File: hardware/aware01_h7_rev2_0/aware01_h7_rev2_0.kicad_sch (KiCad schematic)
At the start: 43 parts, among them J1 Conn_02x07_Odd_Even, J2 Conn_02x05_Odd_Even, U1 LMR50410Y5FQDBVRQ1, U2 LM1117MP-3.3, U4 STM32H7A3RITx, U5 LM4040DIM3X-10, Y1 WE-XTAL 24.0MHz 50ppm

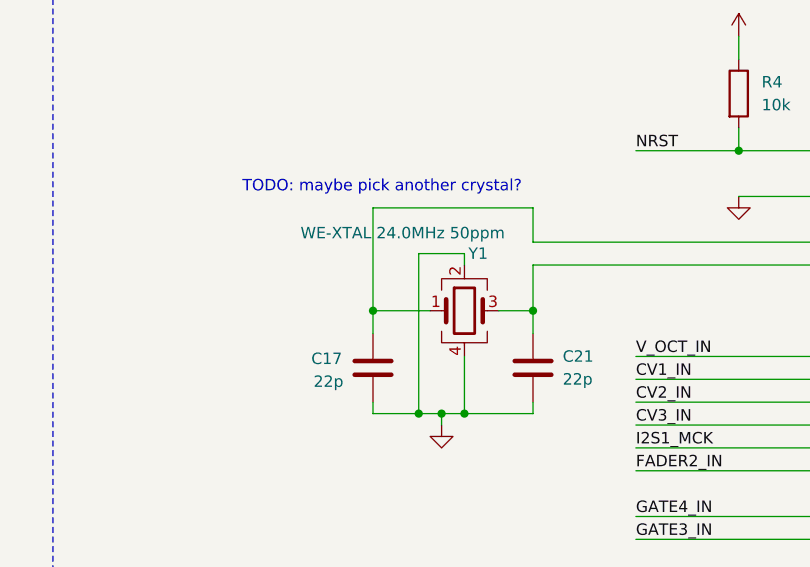
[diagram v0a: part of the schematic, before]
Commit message: hardware: switch crystal and calculate load caps
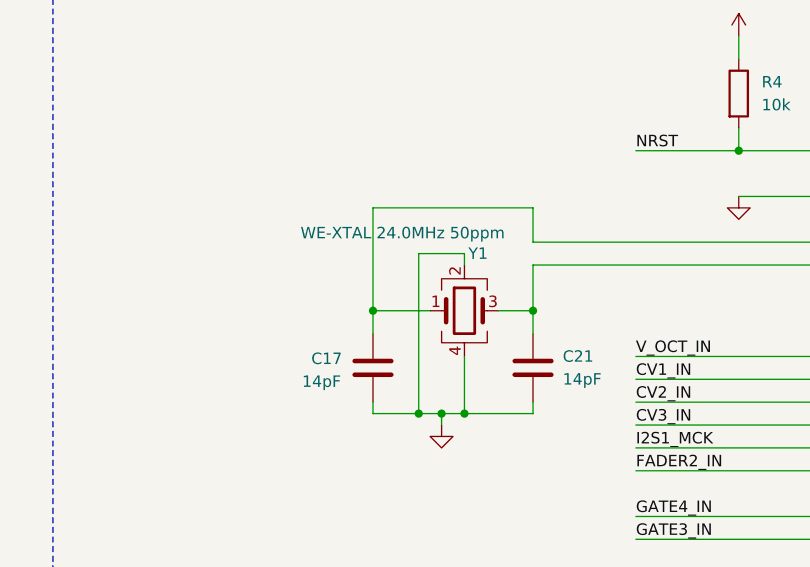
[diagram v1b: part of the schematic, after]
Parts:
- C17, C21: value 22p -> 14pF; footprint Capacitor_SMD:C_0603_1608Metric -> Capacitor_SMD:C_0402_1005Metric_Pad0.74x0.62mm_HandSolder; Manufacturer_Name KEMET -> KYOCERA AVX; Manufacturer_Part_Number C0603C220J1GACTU -> 04023U140GAT2A; Mouser Part Number 80-C0603C220J1G -> 581-04023U140GAT2A
- Y1: footprint Crystal:Crystal_SMD_3225-4Pin_3.2x2.5mm_HandSoldering -> Crystal:Crystal_SMD_2520-4Pin_2.5x2.0mm; Manufacturer_Name Wurth Elektronik -> NDK; Manufacturer_Part_Number 830064703 -> NX2520SA-24.000000MHZ-B8; Mouser Part Number 710-830064703 -> 344-NX2520SA24MHZB8
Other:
- note removed: "TODO: maybe pick another crystal?"
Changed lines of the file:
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@@
 		)
 	)
-	(text "TODO: maybe pick another crystal?"
-		(exclude_from_sim no)
-		(at 150.876 117.094 0)
-		(effects
-			(font
-				(size 1.27 1.27)
-			)
-		)
-	)
 	(text "Power Regulators"
 		(exclude_from_sim no)
@@
 			)
 		)
-		(property "Value" "22p"
-			(at 143.256 138.684 0)
+		(property "Value" "14pF"
+			(at 141.986 138.684 0)
 			(effects
 				(font
@@
 			)
 		)
-		(property "Footprint" "Capacitor_SMD:C_0603_1608Metric"
+		(property "Footprint" "Capacitor_SMD:C_0402_1005Metric_Pad0.74x0.62mm_HandSolder"
 			(at 150.8252 140.97 0)
 			(effects
@@
 			)
 		)
-		(property "Manufacturer_Name" "KEMET "
+		(property "Manufacturer_Name" "KYOCERA AVX "
 			(at 149.86 137.16 0)
 			(effects
@@
 			)
 		)
-		(property "Manufacturer_Part_Number" " C0603C220J1GACTU"
+		(property "Manufacturer_Part_Number" " 04023U140GAT2A "
 			(at 149.86 137.16 0)
 			(effects
@@
 			)
 		)
-		(property "Mouser Part Number" " 80-C0603C220J1G"
+		(property "Mouser Part Number" "581-04023U140GAT2A "
 			(at 149.86 137.16 0)
 			(effects
@@
 			)
 		)
-		(property "Value" "22p"
+		(property "Value" "14pF"
 			(at 170.942 138.43 0)
 			(effects
@@
 			)
 		)
-		(property "Footprint" "Capacitor_SMD:C_0603_1608Metric"
+		(property "Footprint" "Capacitor_SMD:C_0402_1005Metric_Pad0.74x0.62mm_HandSolder"
 			(at 168.6052 140.97 0)
 			(effects
@@
 			)
 		)
-		(property "Manufacturer_Name" "KEMET "
+		(property "Manufacturer_Name" "KYOCERA AVX "
 			(at 167.64 137.16 0)
 			(effects
@@
 			)
 		)
-		(property "Manufacturer_Part_Number" " C0603C220J1GACTU"
+		(property "Manufacturer_Part_Number" " 04023U140GAT2A "
 			(at 167.64 137.16 0)
 			(effects
@@
 			)
 		)
-		(property "Mouser Part Number" " 80-C0603C220J1G"
+		(property "Mouser Part Number" "581-04023U140GAT2A "
 			(at 167.64 137.16 0)
 			(effects
@@
 			)
 		)
-		(property "Footprint" "Crystal:Crystal_SMD_3225-4Pin_3.2x2.5mm_HandSoldering"
+		(property "Footprint" "Crystal:Crystal_SMD_2520-4Pin_2.5x2.0mm"
 			(at 160.02 130.81 0)
 			(effects
@@
 			)
 		)
-		(property "Datasheet" "https://www.we-online.com/components/products/datasheet/830064703.pdf"
+		(property "Datasheet" "https://www.mouser.com/catalog/specsheets/ndk_08142018_NX2520SA-24.000000MHz-B8.pdf"
 			(at 160.02 130.81 0)
 			(effects
@@
 			)
 		)
-		(property "Manufacturer_Name" "Wurth Elektronik"
+		(property "Manufacturer_Name" "NDK"
 			(at 160.02 130.81 0)
 			(effects
@@
 			)
 		)
-		(property "Manufacturer_Part_Number" "830064703 "
+		(property "Manufacturer_Part_Number" " NX2520SA-24.000000MHZ-B8 "
 			(at 160.02 130.81 0)
 			(effects
@@
 			)
 		)
-		(property "Mouser Part Number" " 710-830064703"
+		(property "Mouser Part Number" " 344-NX2520SA24MHZB8 "
 			(at 160.02 130.81 0)
 			(effects

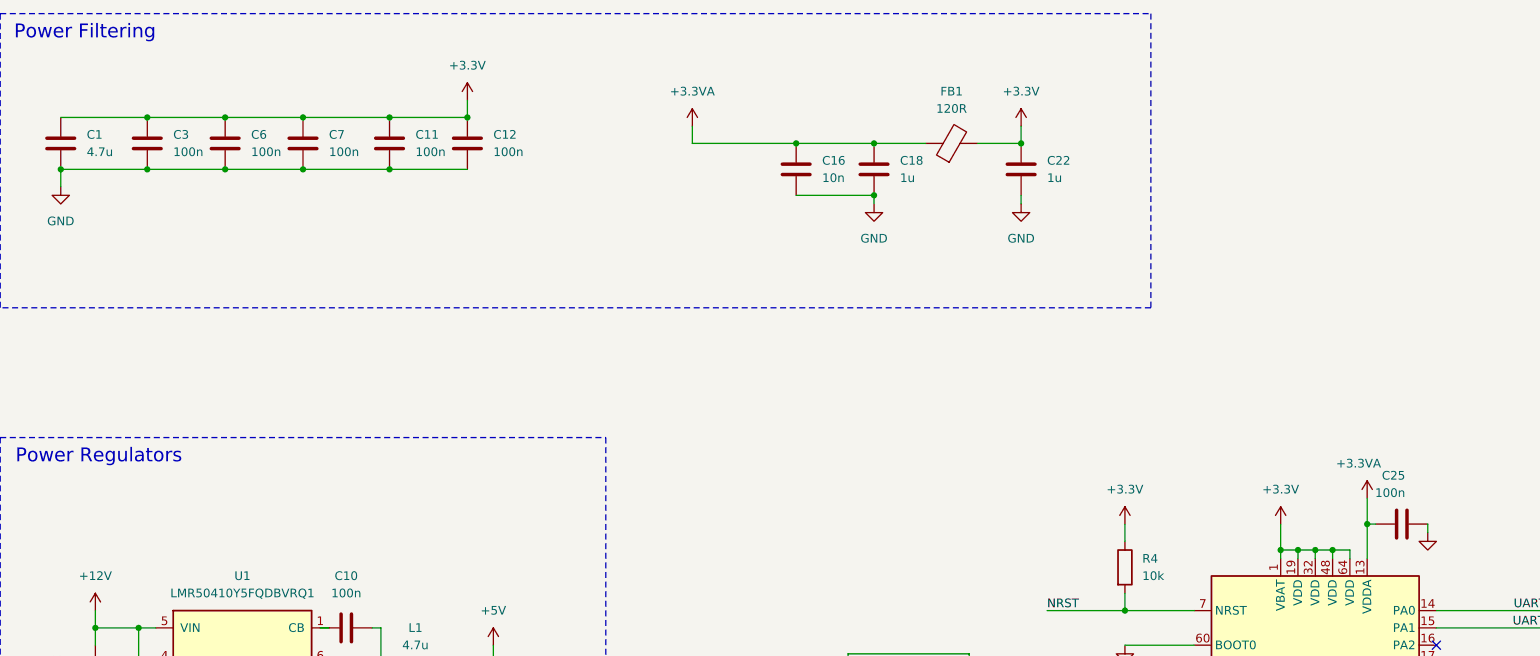
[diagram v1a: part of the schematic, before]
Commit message: hw: improve design after design review (WIP)
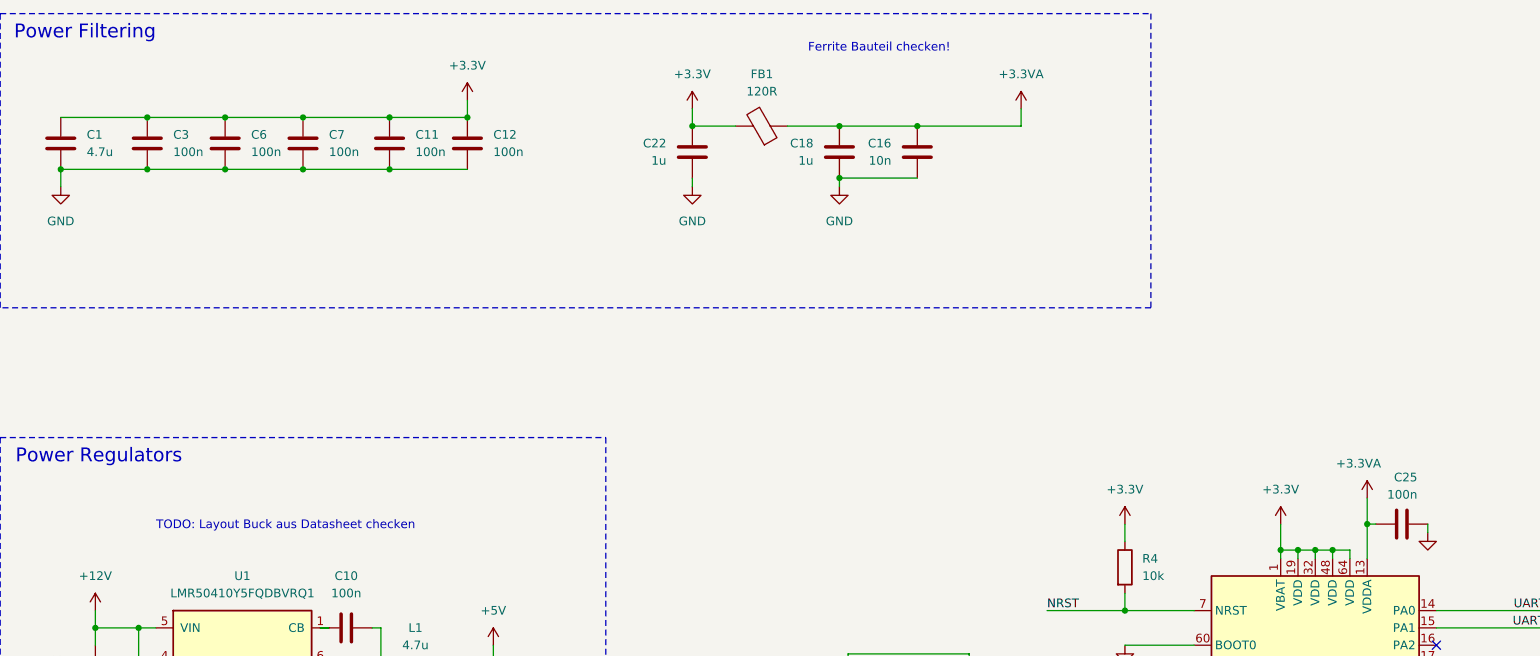
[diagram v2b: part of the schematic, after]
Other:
- note added: "Ferrite Bauteil checken!"
- note added: "TODO: Layout Buck aus Datasheet checken"
- moved on the sheet: C16, C18, C22, FB1

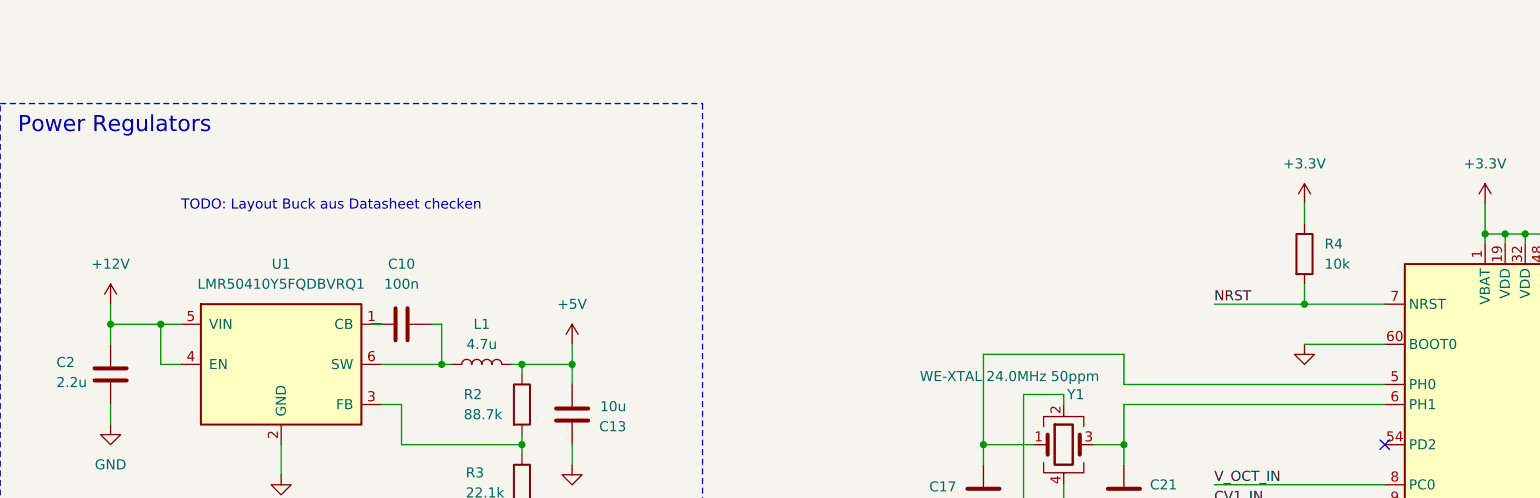
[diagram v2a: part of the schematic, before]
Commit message: hw: improve layout, update BOM
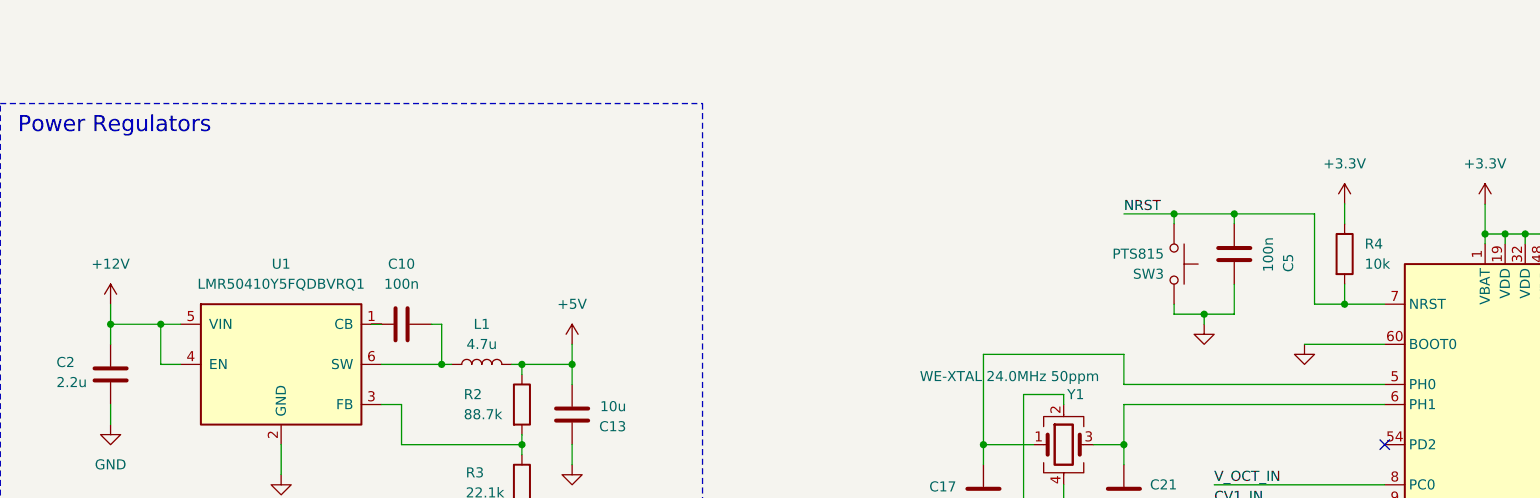
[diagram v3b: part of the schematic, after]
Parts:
- added C5: 100n, Capacitor_SMD:C_0603_1608Metric, symbol Device:C
- added SW3: PTS815, Button_Switch_SMD:SW_SPST_PTS810, symbol Switch:SW_Push
- C10: Manufacturer_Name (none) -> KYOCERA AVX; Manufacturer_Part_Number (none) -> KAF15BR72A104KT; Mouser Part Number (none) -> 581-KAF15BR72A104KT
- C13: Manufacturer_Name (none) -> Murata Electronics; Manufacturer_Part_Number (none) -> GRM188R61E106KA73D; Mouser Part Number (none) -> 81-GRM188R61E106KA3D
- C2: Manufacturer_Name (none) -> TAIYO YUDEN; Manufacturer_Part_Number (none) -> TMK107ABJ225KA-T; Mouser Part Number (none) -> 963-TMK107ABJ225KA-T
- C21: Manufacturer_Name KYOCERA AVX -> KYOCERA AVX; Manufacturer_Part_Number 04023U140GAT2A -> 04023U140GAT2A; Mouser Part Number 581-04023U140GAT2A -> 581-04023U140GAT2A
- FB1: Manufacturer_Part_Number MFBW1V2012-121-R -> MFBW1V2012-121-R; Mouser Part Number 704-MFBW1V2012-121-R -> 704-MFBW1V2012-121-R
- L1: Manufacturer_Name (none) -> Bourns; Manufacturer_Part_Number (none) -> SRR5228A-470M; Mouser Part Number (none) -> 6521-SRR5228A-470M
- R2: Manufacturer_Name (none) -> YAGEO; Manufacturer_Part_Number (none) -> RC0603FR-0788K7L; Mouser Part Number (none) -> 603-RC0603FR-0788K7L
- R3: Manufacturer_Name (none) -> YAGEO; Manufacturer_Part_Number (none) -> RC0603FR-1322K1L; Mouser Part Number (none) -> 603-RC0603FR-1322K1L
- R5, R6: Mouser Part Number 603-RC0603FR-134K7L -> 603-RC0603FR-134K7L
- U1: Manufacturer_Name (none) -> Texas Instruments; Manufacturer_Part_Number (none) -> LMR50410Y5FQDBVRQ1; Mouser Part Number (none) -> 595-R50410Y5FQDBVRQ1
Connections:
- net GND: now also C5.1, SW3.2
- net NRST: now also C5.2, SW3.1
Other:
- note removed: "TODO: Layout Buck aus Datasheet checken"
- moved on the sheet: R4

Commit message: hw: update BOM and layout
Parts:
- added C9: 10u, Capacitor_SMD:C_0603_1608Metric, symbol Device:C
- C13, C4, C8: Manufacturer_Part_Number GRM188R61E106KA73D -> GRM188R61E106KA73D
- C17: Manufacturer_Name KYOCERA AVX -> KYOCERA AVX; Manufacturer_Part_Number 04023U140GAT2A -> 04023U140GAT2A; Mouser Part Number 581-04023U140GAT2A -> 581-04023U140GAT2A
- C18, C22: Manufacturer_Name Walsin -> KYOCERA AVX; Manufacturer_Part_Number 0603B105M160CT -> KGM15AV51A105ZM; Mouser Part Number 791-0603B105M160CT -> 581-KGM15AV51A105ZM
- L1: Manufacturer_Part_Number SRR5228A-470M -> SRR5228A-4R7Y; Mouser Part Number 6521-SRR5228A-470M -> 6521-SRR5228A-4R7Y
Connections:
- net +12V: now also C9.1
- net GND: now also C9.2
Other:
- moved on the sheet: C10, C13, C2, L1, R2, R3, U1

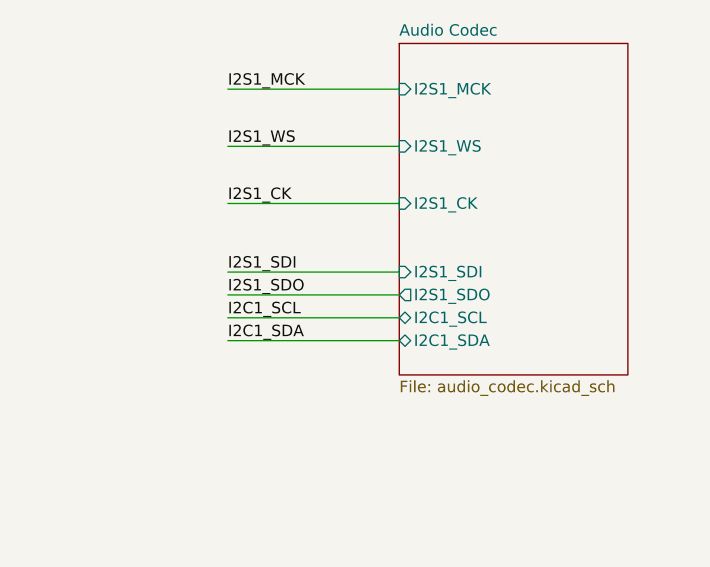
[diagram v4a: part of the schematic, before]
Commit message: hw: add scope screenshots that document buck restart
Which was caused because of short circuit on the MCU pins.
When the LDO received voltage above dropout level, the short draws too
much current and causes the buck to restart.
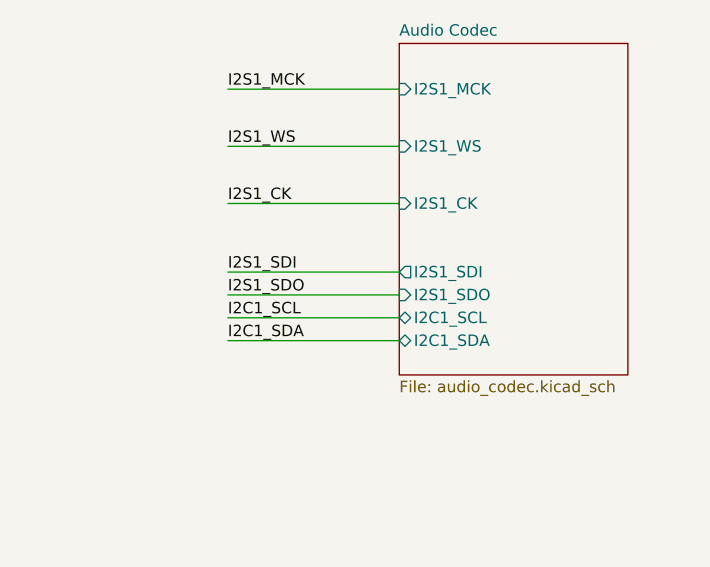
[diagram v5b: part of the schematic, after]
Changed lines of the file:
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@@
 			)
 		)
-		(pin "I2S1_SDO" output
+		(pin "I2S1_SDO" input
 			(at 355.6 217.17 180)
 			(effects
@@
 			)
 		)
-		(pin "I2S1_SDI" input
+		(pin "I2S1_SDI" output
 			(at 355.6 214.63 180)
 			(effects

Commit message: hw: update schematic
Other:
- company: Ausschussware -> Aware Modular
